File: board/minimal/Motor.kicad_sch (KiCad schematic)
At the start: 13 parts, among them IC1 DRV8835DSSR, J3 FR_ESC, J4 FL_ESC, J5 RMotor, J6 LMotor, J7 RR_ESC, J8 RL_ESC, Q1 PMOS, Q2 PMOS

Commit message: update PCB and edit schematic
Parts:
- Q1, Q2: footprint (none) -> Package_TO_SOT_SMD:SOT-223
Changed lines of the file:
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@@
       (effects (font (size 1.27 1.27)))
     )
-    (property "Footprint" "" (at 167.64 100.33 0)
+    (property "Footprint" "Package_TO_SOT_SMD:SOT-223" (at 167.64 100.33 0)
       (effects (font (size 1.27 1.27)) hide)
     )
@@
       (effects (font (size 1.27 1.27)))
     )
-    (property "Footprint" "" (at 185.42 100.33 0)
+    (property "Footprint" "Package_TO_SOT_SMD:SOT-223" (at 185.42 100.33 0)
       (effects (font (size 1.27 1.27)) hide)
     )

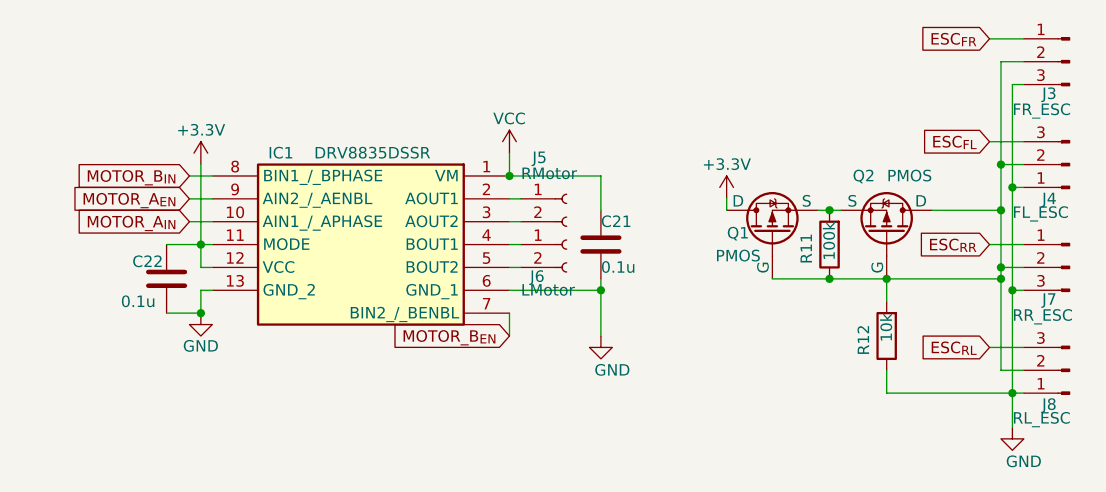
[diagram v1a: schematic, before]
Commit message: add Weather to Dashboard
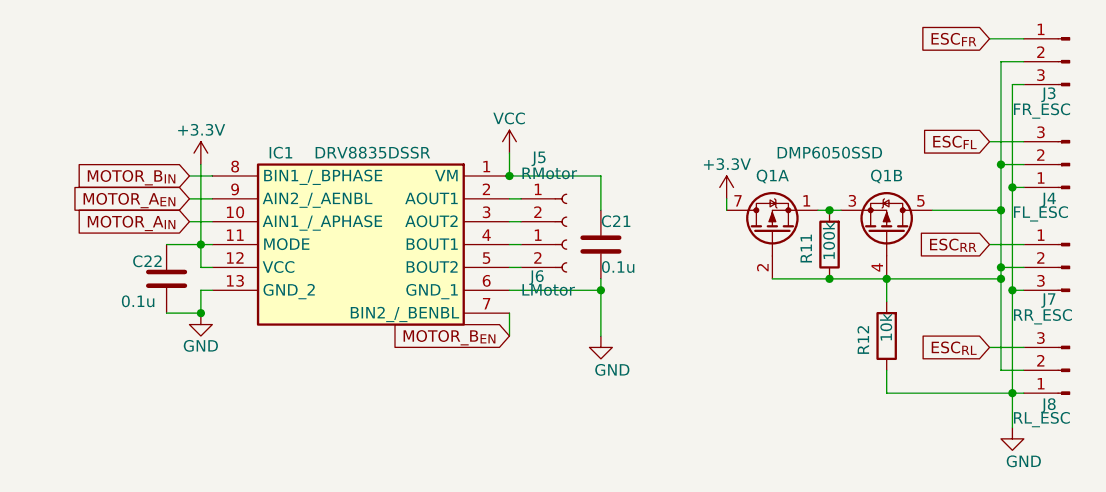
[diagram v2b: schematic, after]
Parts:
- removed Q1, Q2: PMOS, Package_TO_SOT_SMD:SOT-223, symbol Simulation_SPICE:PMOS
- added Q1: DMP6050SSD, Package_SO:SOIC-8_3.9x4.9mm_P1.27mm, symbol Transistor_FET:DMP6050SSD
- C21, C22: footprint Capacitor_SMD:C_0603_1608Metric -> Capacitor_SMD:C_0201_0603Metric
- IC1: footprint DRV8835:DRV8835DSSR -> Package_SON:WSON-12-1EP_3x2mm_P0.5mm_EP1x2.65_ThermalVias
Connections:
- net +3.3V: now also Q1.7 (D1), Q1.8 (D1)
- net at J3.2 (Pin_2), J4.2 (Pin_2), J7.2 (Pin_2)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: now also Q1.2 (G1), Q1.4 (G2), Q1.5 (D2), Q1.6 (D2)
- net at R11.2: now also Q1.1 (S1), Q1.3 (S2)
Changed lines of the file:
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@@
       (effects (font (size 1.27 1.27)))
     )
-    (property "Footprint" "DRV8835:DRV8835DSSR" (at 93.98 193.98 0)
+    (property "Footprint" "Package_SON:WSON-12-1EP_3x2mm_P0.5mm_EP1x2.65_ThermalVias" (at 93.98 193.98 0)
       (effects (font (size 1.27 1.27)) (justify left top) hide)
     )
@@
     )
   )
-  (symbol (lib_id "Simulation_SPICE:PMOS") (at 170.18 105.41 90) (unit 1)
-    (in_bom yes) (on_board yes) (dnp no)
-    (property "Reference" "Q1" (at 166.37 105.41 90)
-      (effects (font (size 1.27 1.27)))
-    )
-    (property "Value" "PMOS" (at 166.37 107.95 90)
-      (effects (font (size 1.27 1.27)))
-    )
-    (property "Footprint" "Package_TO_SOT_SMD:SOT-223" (at 167.64 100.33 0)
-      (effects (font (size 1.27 1.27)) hide)
-    )
-    (property "Datasheet" "https://ngspice.sourceforge.io/docs/ngspice-html-manual/manual.xhtml#cha_MOSFETs" (at 182.88 105.41 0)
-      (effects (font (size 1.27 1.27)) hide)
-    )
-    (property "Sim.Device" "PMOS" (at 187.325 105.41 0)
-      (effects (font (size 1.27 1.27)) hide)
-    )
-    (property "Sim.Type" "VDMOS" (at 189.23 105.41 0)
-      (effects (font (size 1.27 1.27)) hide)
-    )
-    (property "Sim.Pins" "1=D 2=G 3=S" (at 185.42 105.41 0)
-      (effects (font (size 1.27 1.27)) hide)
-    )
-    (pin "1")
-    (pin "2")
-    (pin "3")
-    (instances
-      (project "TurtlePico-Minimal"
-        (path "/7af2d99d-e350-48e7-86b4-20911ea922f3/30a58c44-3c8a-4ad6-a7be-85fee873ce7a"
-          (reference "Q1") (unit 1)
-        )
-      )
-    )
-  )
   (symbol (lib_id "Device:C") (at 151.13 106.68 0) (unit 1)
     (in_bom yes) (on_board yes) (dnp no)
@@
       (effects (font (size 1.27 1.27)) (justify left))
     )
-    (property "Footprint" "Capacitor_SMD:C_0603_1608Metric" (at 152.0952 110.49 0)
+    (property "Footprint" "Capacitor_SMD:C_0201_0603Metric" (at 152.0952 110.49 0)
       (effects (font (size 1.27 1.27)) hide)
     )
@@
     )
   )
-  (symbol (lib_id "Simulation_SPICE:PMOS") (at 182.88 105.41 270) (mirror x) (unit 1)
-    (in_bom yes) (on_board yes) (dnp no)
-    (property "Reference" "Q2" (at 180.34 99.06 90)
-      (effects (font (size 1.27 1.27)))
-    )
-    (property "Value" "PMOS" (at 185.42 99.06 90)
-      (effects (font (size 1.27 1.27)))
-    )
-    (property "Footprint" "Package_TO_SOT_SMD:SOT-223" (at 185.42 100.33 0)
-      (effects (font (size 1.27 1.27)) hide)
-    )
-    (property "Datasheet" "https://ngspice.sourceforge.io/docs/ngspice-html-manual/manual.xhtml#cha_MOSFETs" (at 170.18 105.41 0)
-      (effects (font (size 1.27 1.27)) hide)
-    )
-    (property "Sim.Device" "PMOS" (at 165.735 105.41 0)
-      (effects (font (size 1.27 1.27)) hide)
-    )
-    (property "Sim.Type" "VDMOS" (at 163.83 105.41 0)
-      (effects (font (size 1.27 1.27)) hide)
-    )
-    (property "Sim.Pins" "1=D 2=G 3=S" (at 167.64 105.41 0)
-      (effects (font (size 1.27 1.27)) hide)
-    )
-    (pin "1")
-    (pin "2")
-    (pin "3")
-    (instances
-      (project "TurtlePico-Minimal"
-        (path "/7af2d99d-e350-48e7-86b4-20911ea922f3/30a58c44-3c8a-4ad6-a7be-85fee873ce7a"
-          (reference "Q2") (unit 1)
-        )
-      )
-    )
-  )
   (symbol (lib_id "Device:C") (at 102.87 110.49 0) (unit 1)
     (in_bom yes) (on_board yes) (dnp no)
@@
       (effects (font (size 1.27 1.27)) (justify left))
     )
-    (property "Footprint" "Capacitor_SMD:C_0603_1608Metric" (at 103.8352 114.3 0)
+    (property "Footprint" "Capacitor_SMD:C_0201_0603Metric" (at 103.8352 114.3 0)
       (effects (font (size 1.27 1.27)) hide)
     )
@@
         )
       )
+    )
+  )
+  (symbol (lib_id "Transistor_FET:DMP6050SSD") (at 182.88 105.41 270) (mirror x) (unit 2)
+    (in_bom yes) (on_board yes) (dnp no)
+    (property "Reference" "Q1" (at 182.88 99.06 90)
+      (effects (font (size 1.27 1.27)))
+    )
+    (property "Value" "DMP6050SSD" (at 182.88 99.06 90)
+      (effects (font (size 1.27 1.27)) hide)
+    )
+    (property "Footprint" "Package_SO:SOIC-8_3.9x4.9mm_P1.27mm" (at 180.975 100.33 0)
+      (effects (font (size 1.27 1.27) italic) (justify left) hide)
+    )
+    (property "Datasheet" "https://www.diodes.com/assets/Datasheets/DMP6050SSD.pdf" (at 179.07 100.33 0)
+      (effects (font (size 1.27 1.27)) (justify left) hide)
+    )
+    (pin "7")
+    (pin "2")
+    (pin "1")
+    (pin "3")
+    (pin "5")
+    (pin "4")
+    (pin "6")
+    (pin "8")
+    (instances
+      (project "TurtlePico-Minimal"
+        (path "/7af2d99d-e350-48e7-86b4-20911ea922f3/30a58c44-3c8a-4ad6-a7be-85fee873ce7a"
+          (reference "Q1") (unit 2)
+        )
+      )
+    )
+  )
+  (symbol (lib_id "Transistor_FET:DMP6050SSD") (at 170.18 105.41 90) (unit 1)
+    (in_bom yes) (on_board yes) (dnp no)
+    (property "Reference" "Q1" (at 170.18 99.06 90)
+      (effects (font (size 1.27 1.27)))
+    )
+    (property "Value" "DMP6050SSD" (at 176.53 96.52 90)
+      (effects (font (size 1.27 1.27)))
+    )
+    (property "Footprint" "Package_SO:SOIC-8_3.9x4.9mm_P1.27mm" (at 172.085 100.33 0)
+      (effects (font (size 1.27 1.27) italic) (justify left) hide)
+    )
+    (property "Datasheet" "https://www.diodes.com/assets/Datasheets/DMP6050SSD.pdf" (at 173.99 100.33 0)
+      (effects (font (size 1.27 1.27)) (justify left) hide)
+    )
+    (pin "7")
+    (pin "2")
+    (pin "1")
+    (pin "3")
+    (pin "5")
+    (pin "4")
+    (pin "6")
+    (pin "8")
+    (instances
+      (project "TurtlePico-Minimal"
+        (path "/7af2d99d-e350-48e7-86b4-20911ea922f3/30a58c44-3c8a-4ad6-a7be-85fee873ce7a"
+          (reference "Q1") (unit 1)
+        )
+      )
